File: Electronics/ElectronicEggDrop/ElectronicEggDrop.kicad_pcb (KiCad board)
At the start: 2 copper layers, 52.9 x 74.6 mm, 9 parts

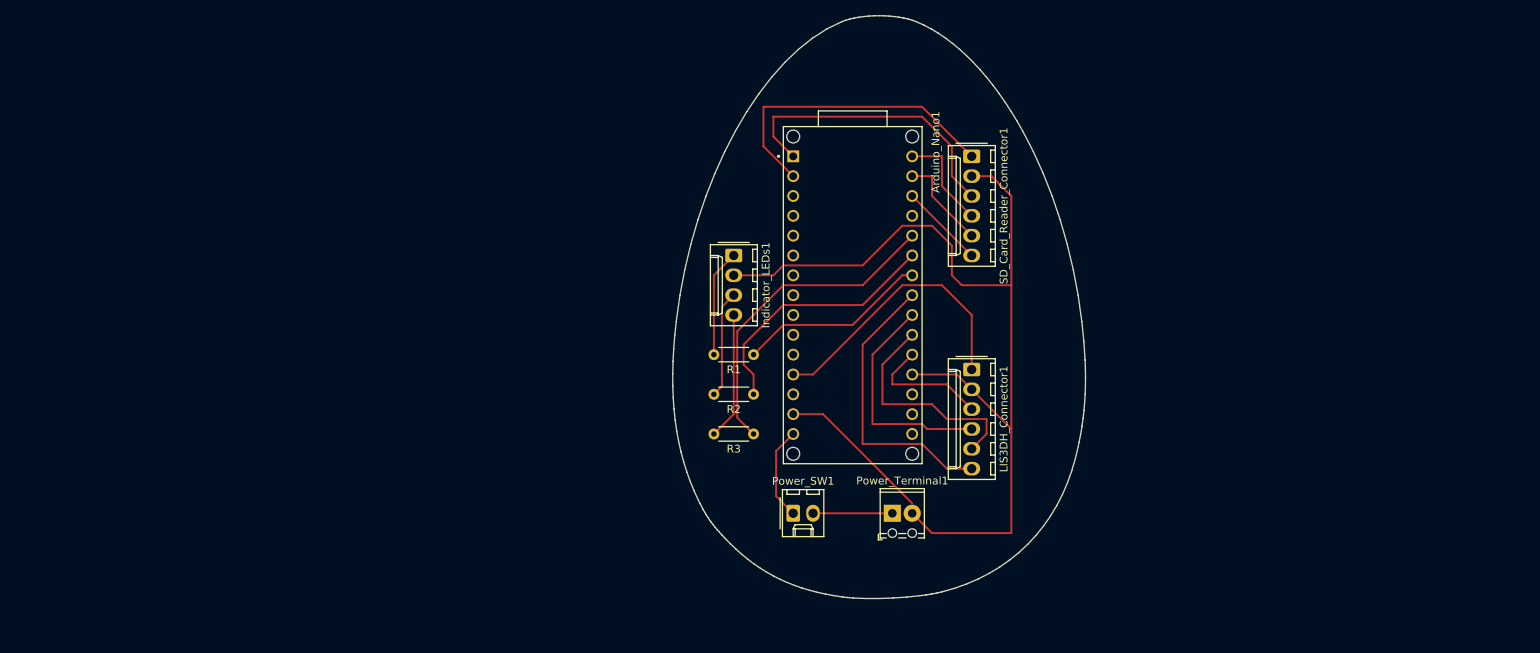
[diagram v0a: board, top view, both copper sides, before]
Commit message: added LIS3DH
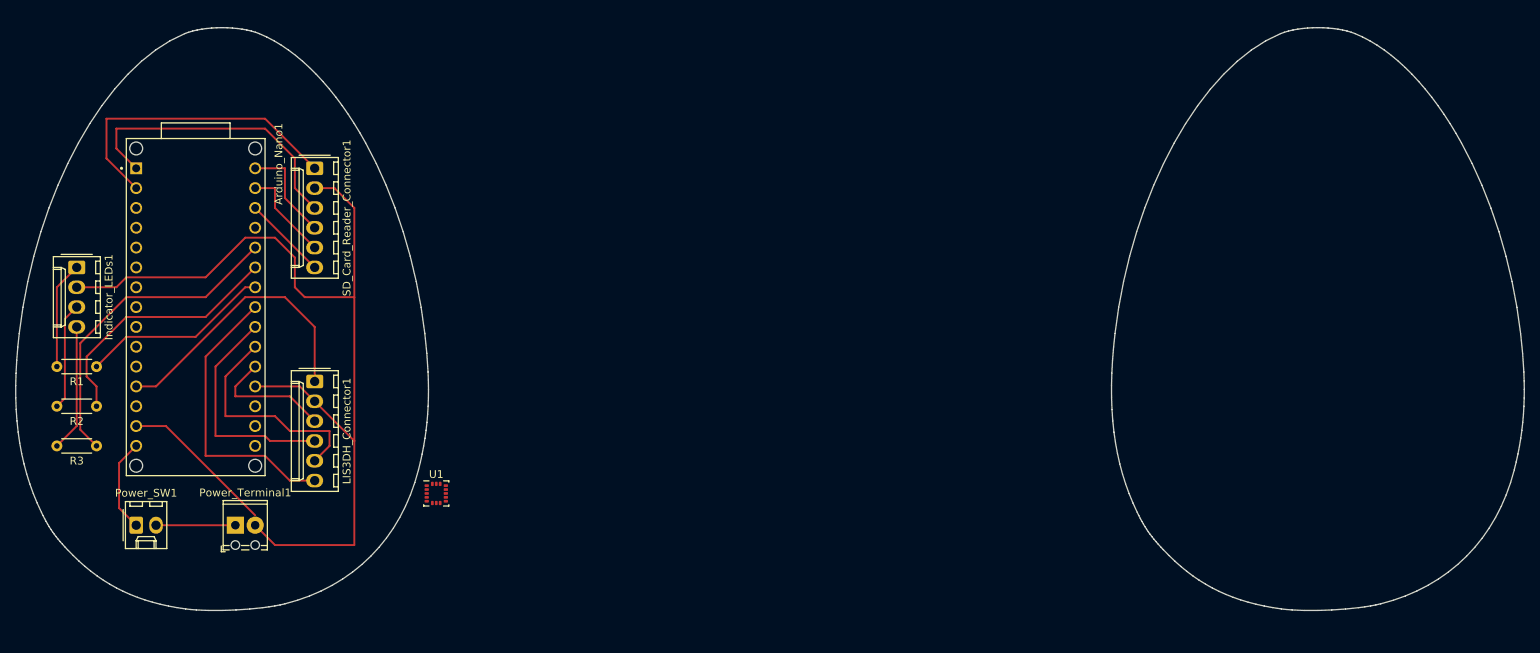
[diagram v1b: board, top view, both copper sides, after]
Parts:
- added U1: LIS3DH, Package_LGA:LGA-16_3x3mm_P0.5mm_LayoutBorder3x5y, F.Cu at (90.8, 126.4)
- moved Arduino_Nano1 84.2 mm to (60.0, 102.5)
- moved Indicator_LEDs1 84.2 mm to (44.7, 97.4)
- moved Power_SW1 84.2 mm to (52.4, 130.4)
- moved R1 84.2 mm to (47.3, 110.1)
- moved R2 84.2 mm to (47.3, 115.2)
- moved R3 84.2 mm to (47.3, 120.3)
- moved LIS3DH_Connector1 84.2 mm to (75.2, 112.0)
- moved Power_Terminal1 84.2 mm to (65.1, 130.4)
- moved SD_Card_Reader_Connector1 84.2 mm to (75.2, 84.7)
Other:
- board size 52.9 x 74.6 mm -> 193.2 x 74.6 mm
- board text added: "Chicken Egg Dinosaurs"
- board text added: "Control Eggcelerometer"
- board text added: "Sensor Eggcelerometer"
- board text added: "What came first, the chicken or the egg?"

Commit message: Finished V1 of the Control and Sensor Egg boards, 3D models created by FreeCAD.  Need to fix code, assemble boards in FreeCAD, and create 3D printed housing
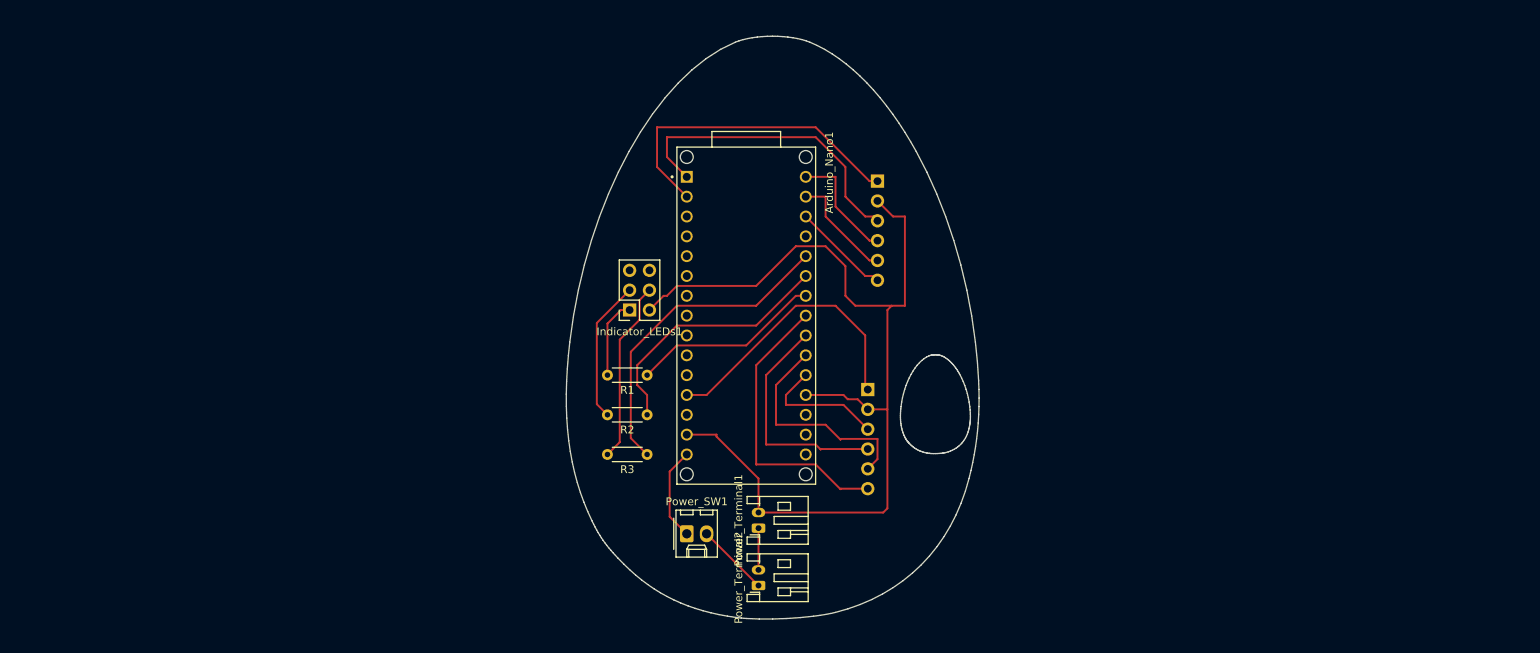
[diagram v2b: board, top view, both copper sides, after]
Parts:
- removed U1: LIS3DH, Package_LGA:LGA-16_3x3mm_P0.5mm_LayoutBorder3x5y
- added Power_Terminal2: Screw_Terminal_01x02, Connector_JST:JST_PH_S2B-PH-K_1x02_P2.00mm_Horizontal, F.Cu at (132.1, 138.2)
- Indicator_LEDs1: footprint Connector_Molex:Molex_KK-254_AE-6410-04A_1x04_P2.54mm_Vertical -> Connector_PinSocket_2.54mm:PinSocket_2x03_P2.54mm_Vertical
- LIS3DH_Connector1, SD_Card_Reader_Connector1: footprint Connector_Molex:Molex_KK-254_AE-6410-06A_1x06_P2.54mm_Vertical -> Connector_PinSocket_2.54mm:PinSocket_1x06_P2.54mm_Vertical; moved to B.Cu
- Power_Terminal1: footprint TerminalBlock_Phoenix:TerminalBlock_Phoenix_MPT-0,5-2-2.54_1x02_P2.54mm_Horizontal -> Connector_JST:JST_PH_S2B-PH-K_1x02_P2.00mm_Horizontal
- moved SD_Card_Reader_Connector1 72.1 mm to (147.3, 86.4), turned to 180 degrees
- moved Indicator_LEDs1 71.0 mm to (115.6, 102.9), turned to 180 degrees
- moved LIS3DH_Connector1 70.9 mm to (146.1, 113.1), turned to 180 degrees
- moved R1 70.5 mm to (117.8, 111.2)
- moved R2 70.5 mm to (117.8, 116.3)
- moved R3 70.5 mm to (117.8, 121.4)
- moved Power_SW1 70.5 mm to (122.9, 131.5)
- moved Arduino_Nano1 70.5 mm to (130.5, 103.6)
- moved Power_Terminal1 67.0 mm to (132.1, 130.8), turned to 90 degrees
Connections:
- Power_Terminal1 pad 1: Net-(Power_SW1-Pad2) -> Net-(Power_Terminal1-Pad1)
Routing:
- net GND: track 142.2 -> 127.4 mm
- net Net-(Indicator_LEDs1-Pad4): track 16.3 -> 23.3 mm
- net Net-(Power_Terminal1-Pad1): track 0.00 -> 5.35 mm
- net Net-(Indicator_LEDs1-Pad3): track 13.8 -> 18.3 mm
- net Net-(Indicator_LEDs1-Pad1): track 13.8 -> 10.2 mm
- net Net-(Arduino_Nano1-Pad1): track 38.0 -> 39.8 mm
- net Net-(Arduino_Nano1-Pad30): track 13.0 -> 14.8 mm
- net Net-(Arduino_Nano1-Pad28): track 10.8 -> 12.6 mm
- net Net-(Arduino_Nano1-Pad2): track 39.8 -> 41.6 mm
- net Net-(Arduino_Nano1-Pad29): track 12.3 -> 14.1 mm
- net Net-(Power_SW1-Pad2): track 10.2 -> 9.39 mm
- net Net-(Arduino_Nano1-Pad21): track 29.2 -> 28.6 mm
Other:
- board size 193.2 x 74.6 mm -> 52.9 x 74.6 mm
- board text removed: "Sensor Eggcelerometer"

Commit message: Finished the PCBs
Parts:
- added REF**: MountingHole_2.2mm_M2_DIN965_Pad, MountingHole:MountingHole_2.2mm_M2_DIN965_Pad, F.Cu at (116.8, 129.5)
- added REF**: MountingHole_2.2mm_M2_DIN965_Pad, MountingHole:MountingHole_2.2mm_M2_DIN965_Pad, F.Cu at (116.8, 88.9)
- Arduino Nano: renamed from Arduino_Nano1
- LIS3DH Connector: renamed from LIS3DH_Connector1
- SD Card Reader Connector: renamed from SD_Card_Reader_Connector1
- Switch: renamed from Power_SW1; footprint Connector_Molex:Molex_KK-254_AE-6410-02A_1x02_P2.54mm_Vertical -> Connector_PinSocket_2.54mm:PinSocket_1x02_P2.54mm_Vertical
- moved Switch 3.24 mm to (121.9, 134.6), turned to 90 degrees
- renumbered Power_Terminal1 to +3.7V, Power_Terminal2 to +3.7v
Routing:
- net Net-(Arduino_Nano1-Pad15): track 12.0 -> 16.0 mm
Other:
- board text added: "M2"
